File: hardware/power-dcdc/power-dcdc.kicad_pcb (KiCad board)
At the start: 2 copper layers, 110 x 70 mm, 69 parts, among them J1 SOLAR_IN, J2 DCDC-MEASURES, J3 DCDC-PWM, J4 BATT2, J5 BATT1, Q1 SIR164ADP, Q2 SIR164ADP, Q3 SI7149ADP, Q4 SI7149ADP, Q5 SI7149ADP, Q6 SI7149ADP, U1 LP4951C, U2 NCP5901B, U3 PAC1953-1, U4 DGD0215, U5 DGD0215

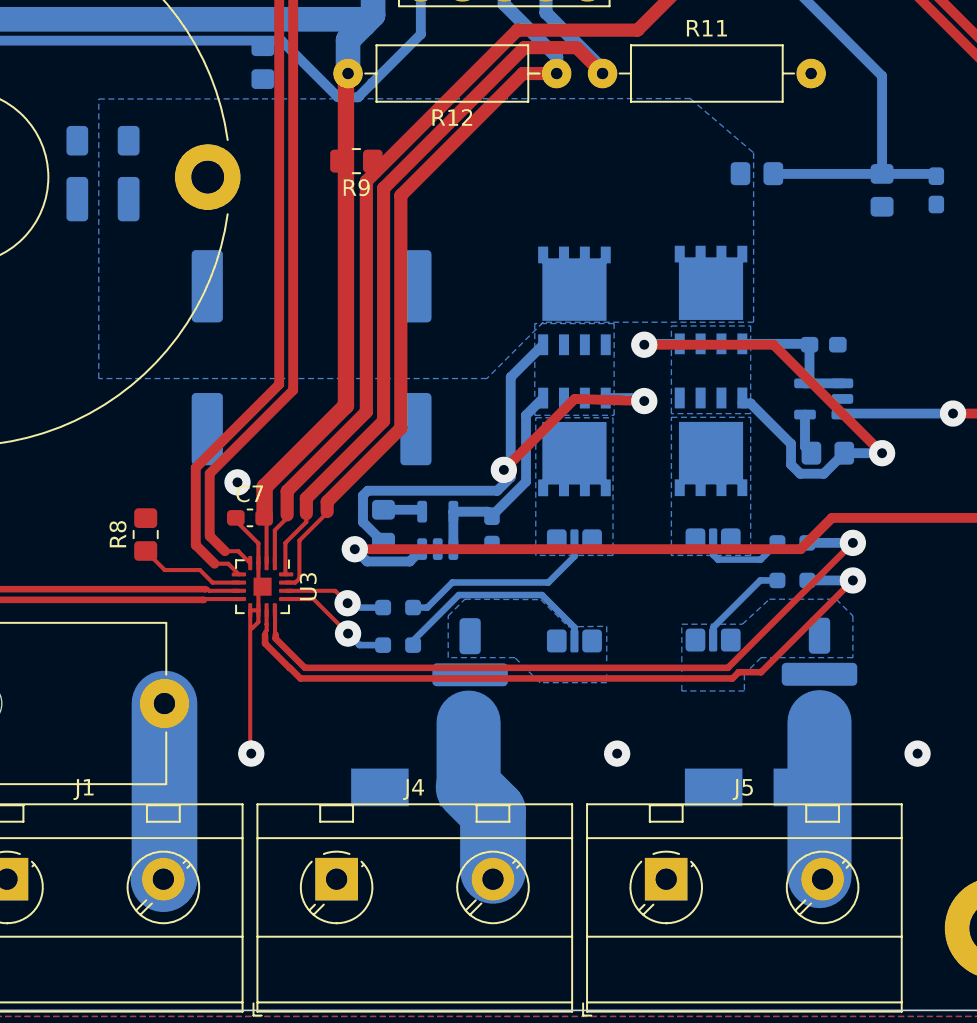
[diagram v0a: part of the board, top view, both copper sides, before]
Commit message: power-dcdc: more track adjusteemnts
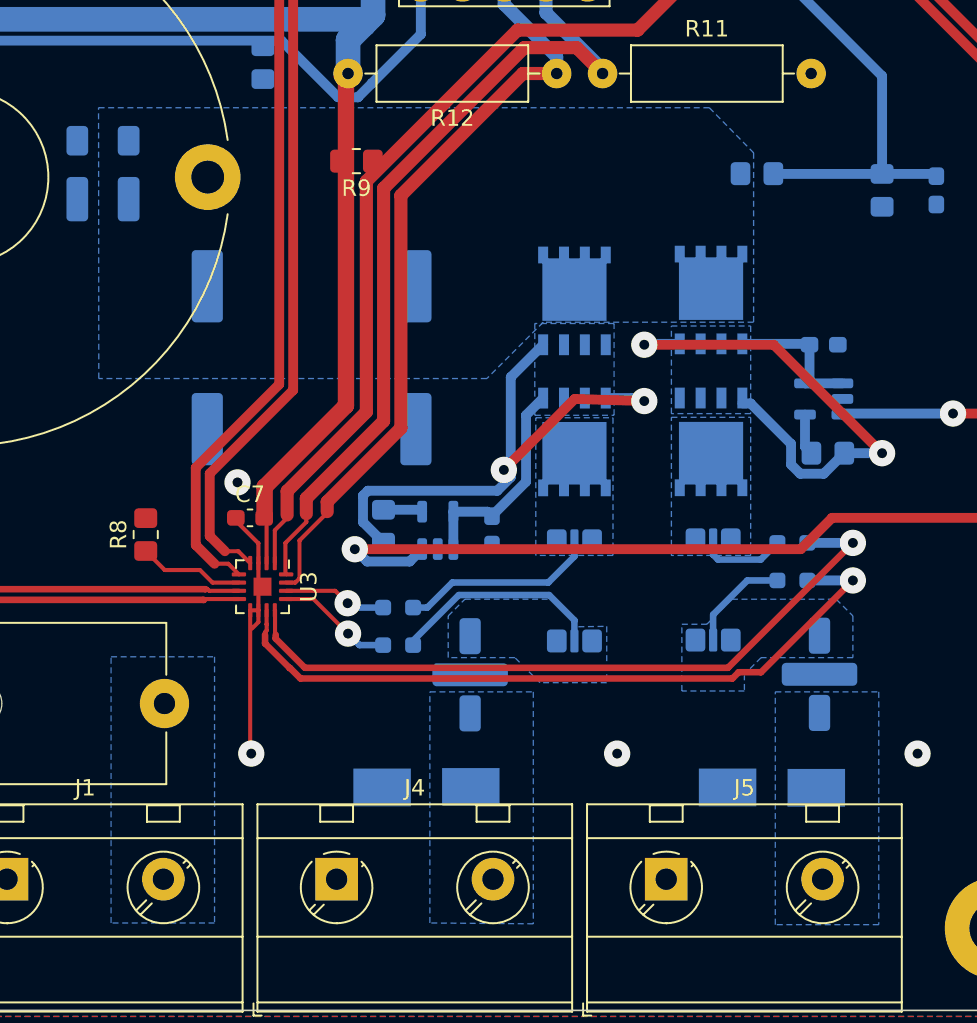
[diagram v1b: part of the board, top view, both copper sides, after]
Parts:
- moved D3 0.85 mm to (141.4, 136.4)
- moved D2 0.14 mm to (120.3, 136.4)
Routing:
- net Net-(F1-Pad1): track 10.7 -> 0.00 mm
- net Net-(C15-Pad1): track 9.64 -> 0.00 mm
- net Net-(C16-Pad1): track 9.38 -> 0.00 mm
- added copper zone on B.Cu, net Net-(C15-Pad1)
- added copper zone on B.Cu, net Net-(C16-Pad1)
- added copper zone on B.Cu, net Net-(F1-Pad1)
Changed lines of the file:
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@@
   )
   (footprint "Diode_SMD:D_SMB_Handsoldering" (layer "B.Cu")
-    (at 120.208 136.426 180)
+    (at 120.3452 136.398 180)
     (descr "Diode SMB (DO-214AA) Handsoldering")
     (tags "Diode SMB (DO-214AA) Handsoldering")
@@
     (pad "1" smd rect (at -2.7 0 180) (size 3.5 2.3) (layers "B.Cu" "B.Paste" "B.Mask")
       (net 8 "Net-(C15-Pad1)") (pinfunction "A1") (pintype "passive"))
-    (pad "2" smd rect (at 2.7 0 180) (size 3.5 2.3) (layers "B.Cu" "B.Paste" "B.Mask")
+    (pad "2" smd rect (at 2.7 -0.028 180) (size 3.5 2.3) (layers "B.Cu" "B.Paste" "B.Mask")
       (net 2 "GND") (pinfunction "A2") (pintype "passive") (zone_connect 2))
     (model "${KICAD6_3DMODEL_DIR}/Diode_SMD.3dshapes/D_SMB.wrl"
@@
   )
   (footprint "Diode_SMD:D_SMB_Handsoldering" (layer "B.Cu")
-    (at 140.528 136.426 180)
+    (at 141.3764 136.4488 180)
     (descr "Diode SMB (DO-214AA) Handsoldering")
     (tags "Diode SMB (DO-214AA) Handsoldering")
@@
     (pad "1" smd rect (at -2.7 0 180) (size 3.5 2.3) (layers "B.Cu" "B.Paste" "B.Mask")
       (net 12 "Net-(C16-Pad1)") (pinfunction "A1") (pintype "passive"))
-    (pad "2" smd rect (at 2.7 0 180) (size 3.5 2.3) (layers "B.Cu" "B.Paste" "B.Mask")
+    (pad "2" smd rect (at 2.7 0.0228 180) (size 3.5 2.3) (layers "B.Cu" "B.Paste" "B.Mask")
       (net 2 "GND") (pinfunction "A2") (pintype "passive") (zone_connect 2))
     (model "${KICAD6_3DMODEL_DIR}/Diode_SMD.3dshapes/D_SMB.wrl"
@@
   (segment (start 115.57 92.964) (end 115.57 90.932) (width 1.5) (layer "B.Cu") (net 5))
   (segment (start 85.598 99.4175) (end 85.598 90.4748) (width 0.6) (layer "B.Cu") (net 5))
-  (segment (start 122.908 136.426) (end 122.908 132.478) (width 3.9) (layer "B.Cu") (net 8))
-  (segment (start 124.394 137.912) (end 122.908 136.426) (width 4) (layer "B.Cu") (net 8))
-  (segment (start 124.394 141.506) (end 124.394 137.912) (width 4) (layer "B.Cu") (net 8))
   (segment (start 67.056 133.7056) (end 66.2686 134.493) (width 1) (layer "F.Cu") (net 9))
   (segment (start 53.2765 125.222) (end 61.946 125.222) (width 1) (layer "F.Cu") (net 9))
@@
   (segment (start 121.981 119.6395) (end 124.058 119.6395) (width 0.6) (layer "B.Cu") (net 11))
   (segment (start 124.333 119.888) (end 126.4055 117.8155) (width 0.6) (layer "B.Cu") (net 11))
-  (segment (start 144.272 141.826) (end 144.272 132.45) (width 3.9) (layer "B.Cu") (net 12))
   (segment (start 143.6635 109.474) (end 143.6635 111.551) (width 0.6) (layer "B.Cu") (net 13))
   (segment (start 143.3885 111.826) (end 145.6635 111.826) (width 0.6) (layer "B.Cu") (net 13))
   (segment (start 143.6635 111.551) (end 143.3885 111.826) (width 0.6) (layer "B.Cu") (net 13))
   (segment (start 139.573 109.422) (end 143.6115 109.422) (width 0.6) (layer "B.Cu") (net 13))
-  (segment (start 104.394 131.318) (end 104.394 141.948) (width 4) (layer "B.Cu") (net 14))
-  (segment (start 104.394 141.948) (end 104.328 142.014) (width 4) (layer "B.Cu") (net 14))
   (segment (start 108.9255 124.456) (end 107.111894 124.456) (width 0.25) (layer "F.Cu") (net 16))
   (segment (start 107.111894 124.456) (end 107.013894 124.358) (width 0.25) (layer "F.Cu") (net 16))
@@
   (segment (start 115.8071 125.476) (end 117.7055 125.476) (width 0.4) (layer "B.Cu") (net 27))
   (segment (start 115.542305 125.211205) (end 115.8071 125.476) (width 0.4) (layer "B.Cu") (net 27))
-  (segment (start 129.352 126.685) (end 127.381 124.714) (width 0.4) (layer "B.Cu") (net 28))
-  (segment (start 127.381 124.714) (end 122.31275 124.714) (width 0.4) (layer "B.Cu") (net 28))
   (segment (start 122.31275 124.714) (end 119.5305 127.49625) (width 0.4) (layer "B.Cu") (net 28))
-  (segment (start 129.352 127.51) (end 129.352 126.685) (width 0.4) (layer "B.Cu") (net 28))
+  (segment (start 127.8128 124.714) (end 122.31275 124.714) (width 0.4) (layer "B.Cu") (net 28))
+  (segment (start 129.352 126.2532) (end 127.8128 124.714) (width 0.4) (layer "B.Cu") (net 28))
+  (segment (start 129.352 127.51) (end 129.352 126.2532) (width 0.4) (layer "B.Cu") (net 28))
   (segment (start 115.57 127.0605) (end 113.4655 124.956) (width 0.25) (layer "F.Cu") (net 29))
   (segment (start 113.4655 124.956) (end 111.8005 124.956) (width 0.25) (layer "F.Cu") (net 29))
@@
   (via (at 146.304 121.539) (size 1.6) (drill 0.6) (layers "F.Cu" "B.Cu") (net 31))
   (segment (start 143.5335 121.539) (end 146.304 121.539) (width 0.6) (layer "B.Cu") (net 31))
-  (segment (start 137.795 126.697499) (end 140.667499 123.825) (width 0.4) (layer "B.Cu") (net 32))
-  (segment (start 137.795 127.455) (end 137.795 126.697499) (width 0.4) (layer "B.Cu") (net 32))
-  (segment (start 140.667499 123.825) (end 141.7085 123.825) (width 0.4) (layer "B.Cu") (net 32))
+  (segment (start 137.795 127.455) (end 137.795 125.9078) (width 0.4) (layer "B.Cu") (net 32))
+  (segment (start 137.795 125.9078) (end 139.8778 123.825) (width 0.4) (layer "B.Cu") (net 32))
+  (segment (start 139.8778 123.825) (end 141.7085 123.825) (width 0.4) (layer "B.Cu") (net 32))
   (segment (start 110.613 126.488) (end 110.617 126.492) (width 0.25) (layer "F.Cu") (net 33))
   (segment (start 110.617 126.873) (end 110.514999 126.975001) (width 0.25) (layer "F.Cu") (net 33))
@@
     )
   )
+  (zone (net 8) (net_name "Net-(C15-Pad1)") (layer "B.Cu") (hatch edge 0.508)
+    (priority 3)
+    (connect_pads yes (clearance 0.39))
+    (min_thickness 0.254) (filled_areas_thickness no)
+    (fill yes (thermal_gap 0.508) (thermal_bridge_width 0.508) (smoothing fillet) (radius 0.2))
+    (polygon
+      (pts
+        (xy 126.8476 144.7292)
+        (xy 120.5484 144.6784)
+        (xy 120.5484 130.6068)
+        (xy 126.8476 130.6068)
+      )
+    )
+  )
+  (zone (net 14) (net_name "Net-(F1-Pad1)") (layer "B.Cu") (hatch edge 0.508)
+    (priority 3)
+    (connect_pads yes (clearance 0.39))
+    (min_thickness 0.254) (filled_areas_thickness no)
+    (fill yes (thermal_gap 0.508) (thermal_bridge_width 0.508) (smoothing fillet) (radius 0.2))
+    (polygon
+      (pts
+        (xy 107.442 144.6784)
+        (xy 101.1428 144.6784)
+        (xy 101.1428 128.4732)
+        (xy 107.442 128.4732)
+      )
+    )
+  )
   (zone (net 1) (net_name "Net-(C1-Pad3)") (layer "B.Cu") (hatch edge 0.508)
     (priority 3)
@@
         (xy 124.018 111.534)
         (xy 100.396 111.534)
-        (xy 100.396 94.516)
-        (xy 136.398 94.488)
+        (xy 100.3808 95.0468)
+        (xy 137.5664 95.0468)
       )
     )
@@
         (xy 135.89 130.556)
         (xy 135.89 126.492)
-        (xy 139.573 126.492)
-        (xy 141.224 124.968)
+        (xy 137.414 126.492)
+        (xy 138.938 124.968)
         (xy 145.288 124.968)
       )
@@
     )
   )
+  (zone (net 12) (net_name "Net-(C16-Pad1)") (layer "B.Cu") (hatch edge 0.508)
+    (priority 3)
+    (connect_pads yes (clearance 0.39))
+    (min_thickness 0.254) (filled_areas_thickness no)
+    (fill yes (thermal_gap 0.508) (thermal_bridge_width 0.508) (smoothing fillet) (radius 0.2))
+    (polygon
+      (pts
+        (xy 147.8788 144.78)
+        (xy 141.5796 144.78)
+        (xy 141.5796 130.6068)
+        (xy 147.8788 130.6068)
+      )
+    )
+  )
   (zone (net 11) (net_name "Net-(C17-Pad1)") (layer "B.Cu") (hatch edge 0.508)
     (priority 2)
@@
         (xy 121.666 125.984)
         (xy 122.682 124.968)
-        (xy 127.3048 124.9934)
-        (xy 128.9812 126.6444)
+        (xy 127.9652 124.968)
+        (xy 129.5908 126.6444)
         (xy 131.318 126.619)
       )

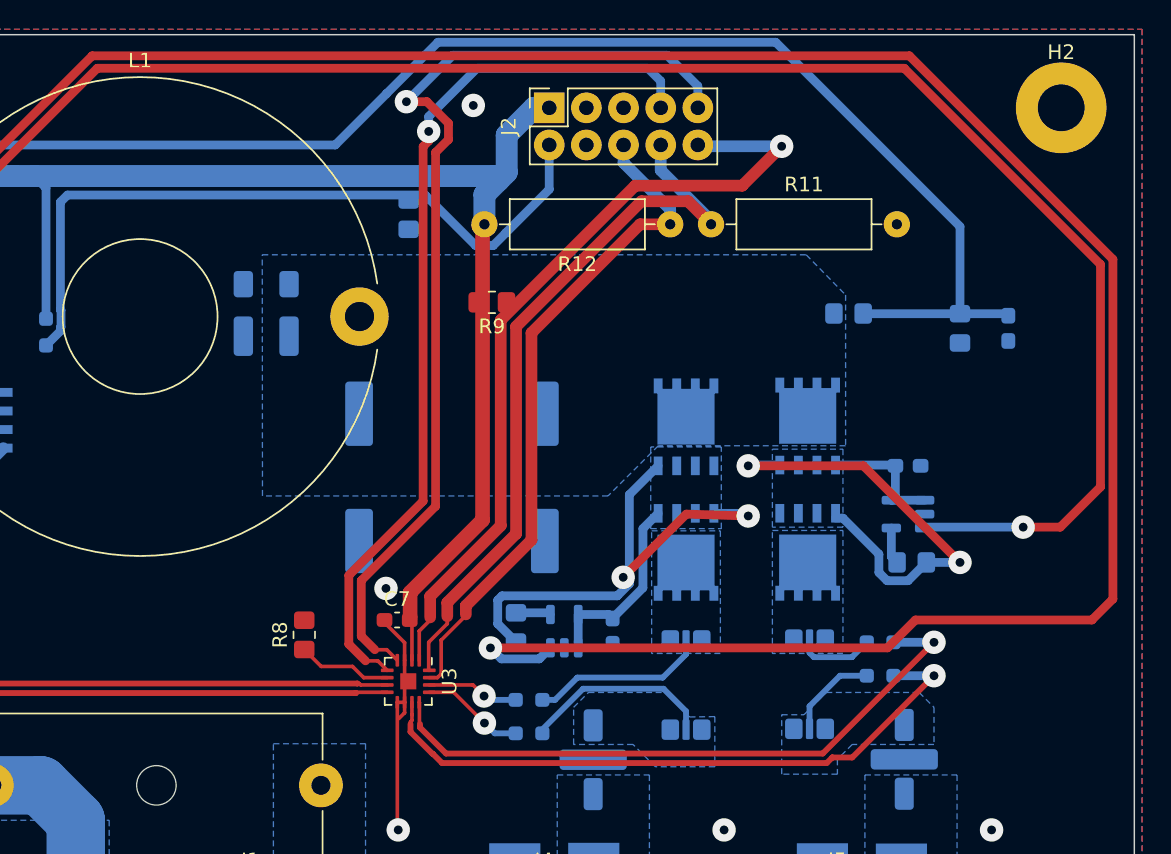
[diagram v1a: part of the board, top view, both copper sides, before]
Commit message: *: connect unused connectors pins to GND
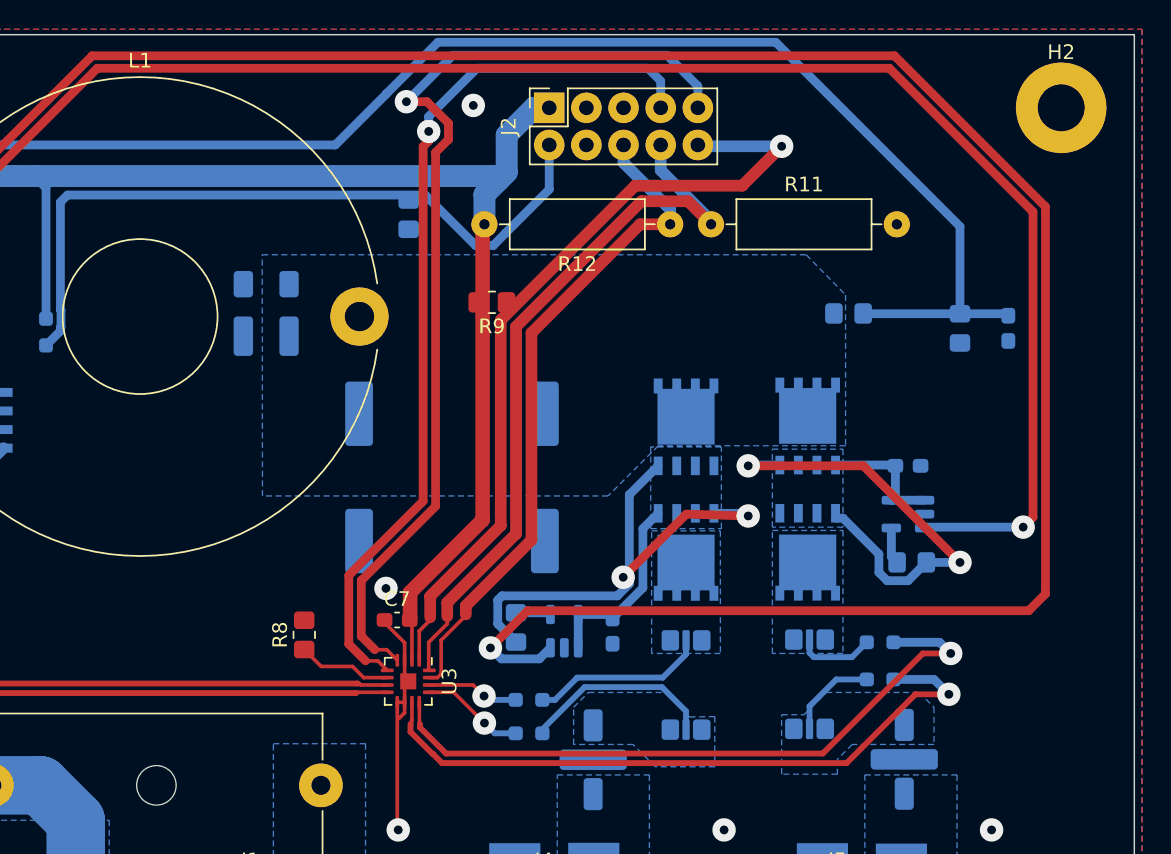
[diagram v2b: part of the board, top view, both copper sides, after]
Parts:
- moved F7 0.25 mm to (142.6, 124.1)
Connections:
- J2 pad 4: unconnected-(J2-Pad4) -> GND
- J2 pad 5: unconnected-(J2-Pad5) -> GND
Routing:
- net BATT2_ON: track 193.2 -> 185.8 mm
- net BATT1_ON: track 141.1 -> 135.2 mm
- net Net-(F6-Pad2): track 43.5 -> 45.8 mm
- net Net-(F7-Pad2): track 44.0 -> 46.0 mm

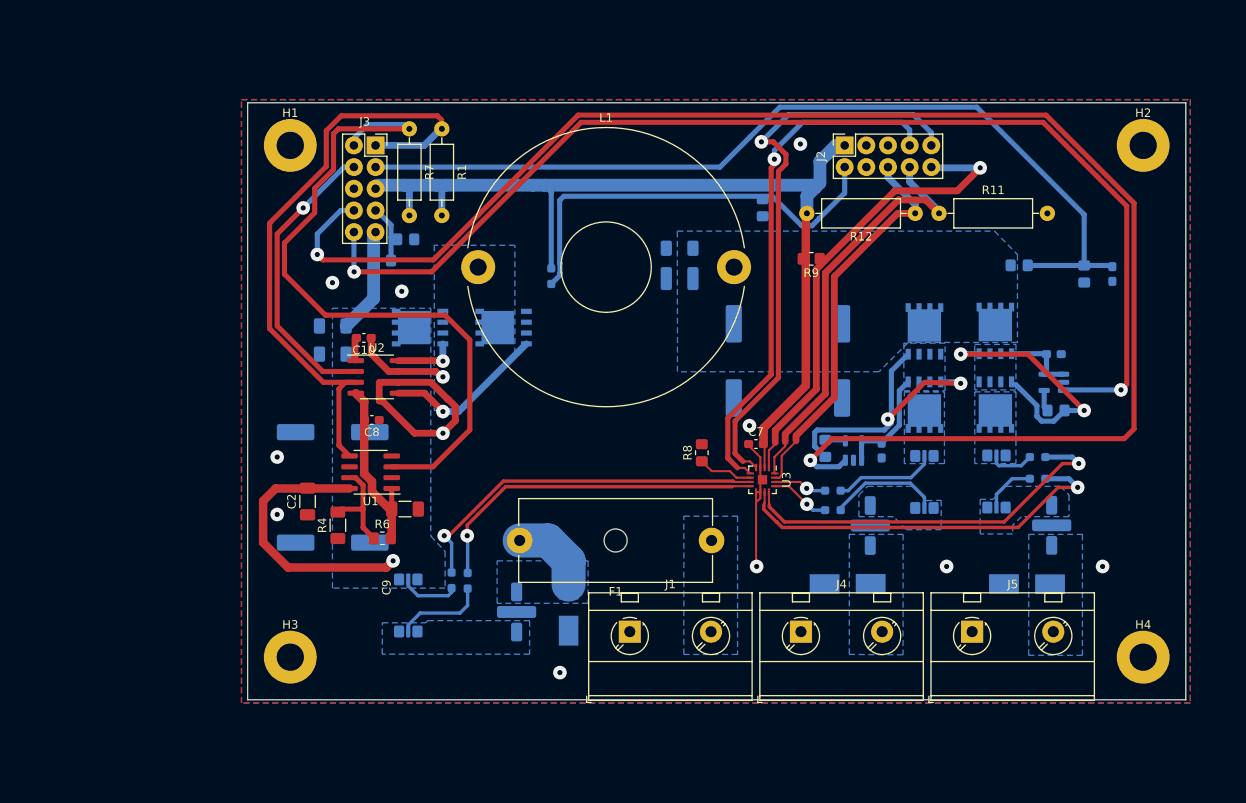
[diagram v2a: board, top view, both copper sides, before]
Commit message: Increase clearance once again
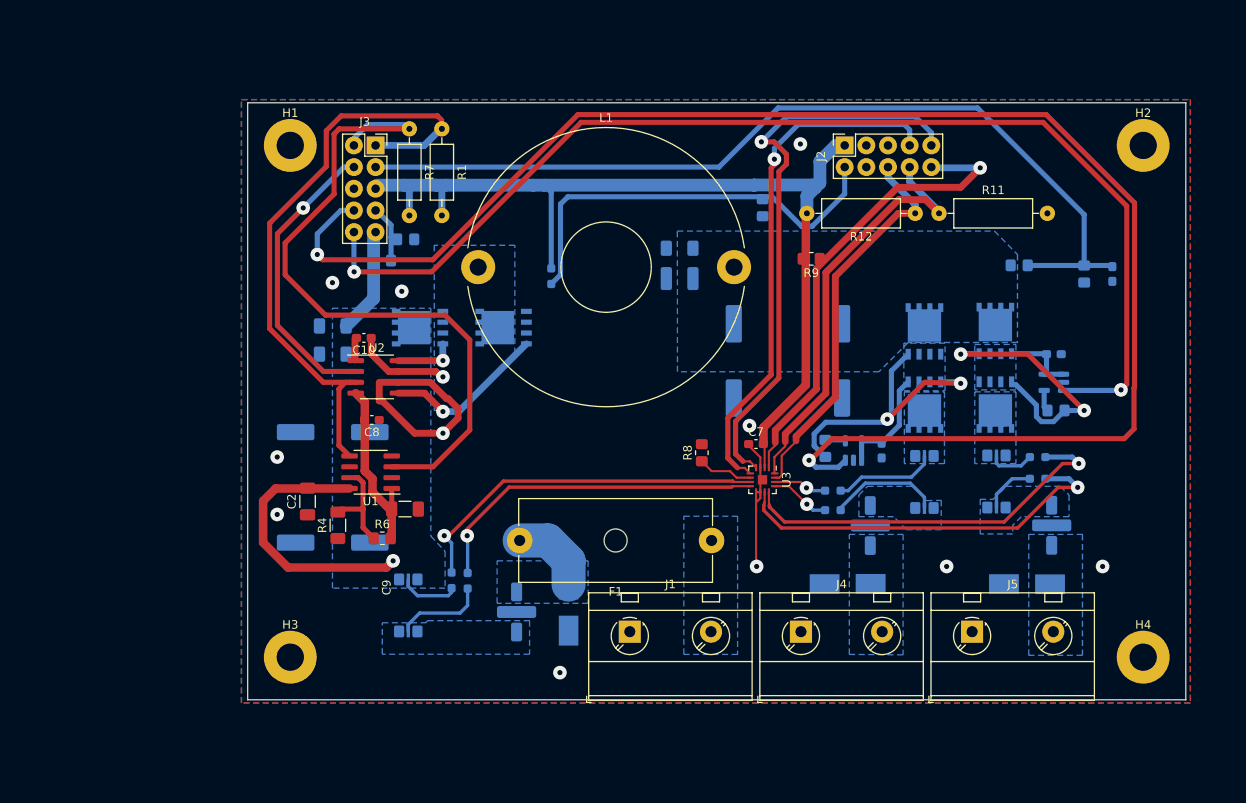
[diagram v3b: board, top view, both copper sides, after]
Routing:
- net BATT2_ON: track 185.8 -> 186.3 mm

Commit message: Add fabrication files
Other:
- board size 110 x 70 mm -> 120 x 90 mm
